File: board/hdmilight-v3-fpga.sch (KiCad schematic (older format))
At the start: 47 parts, among them J3 Conn_01x02_Male, U5 XC6SLX9-TQG144, U7 S25FL064L, X1 SG-310SCF-32MHz

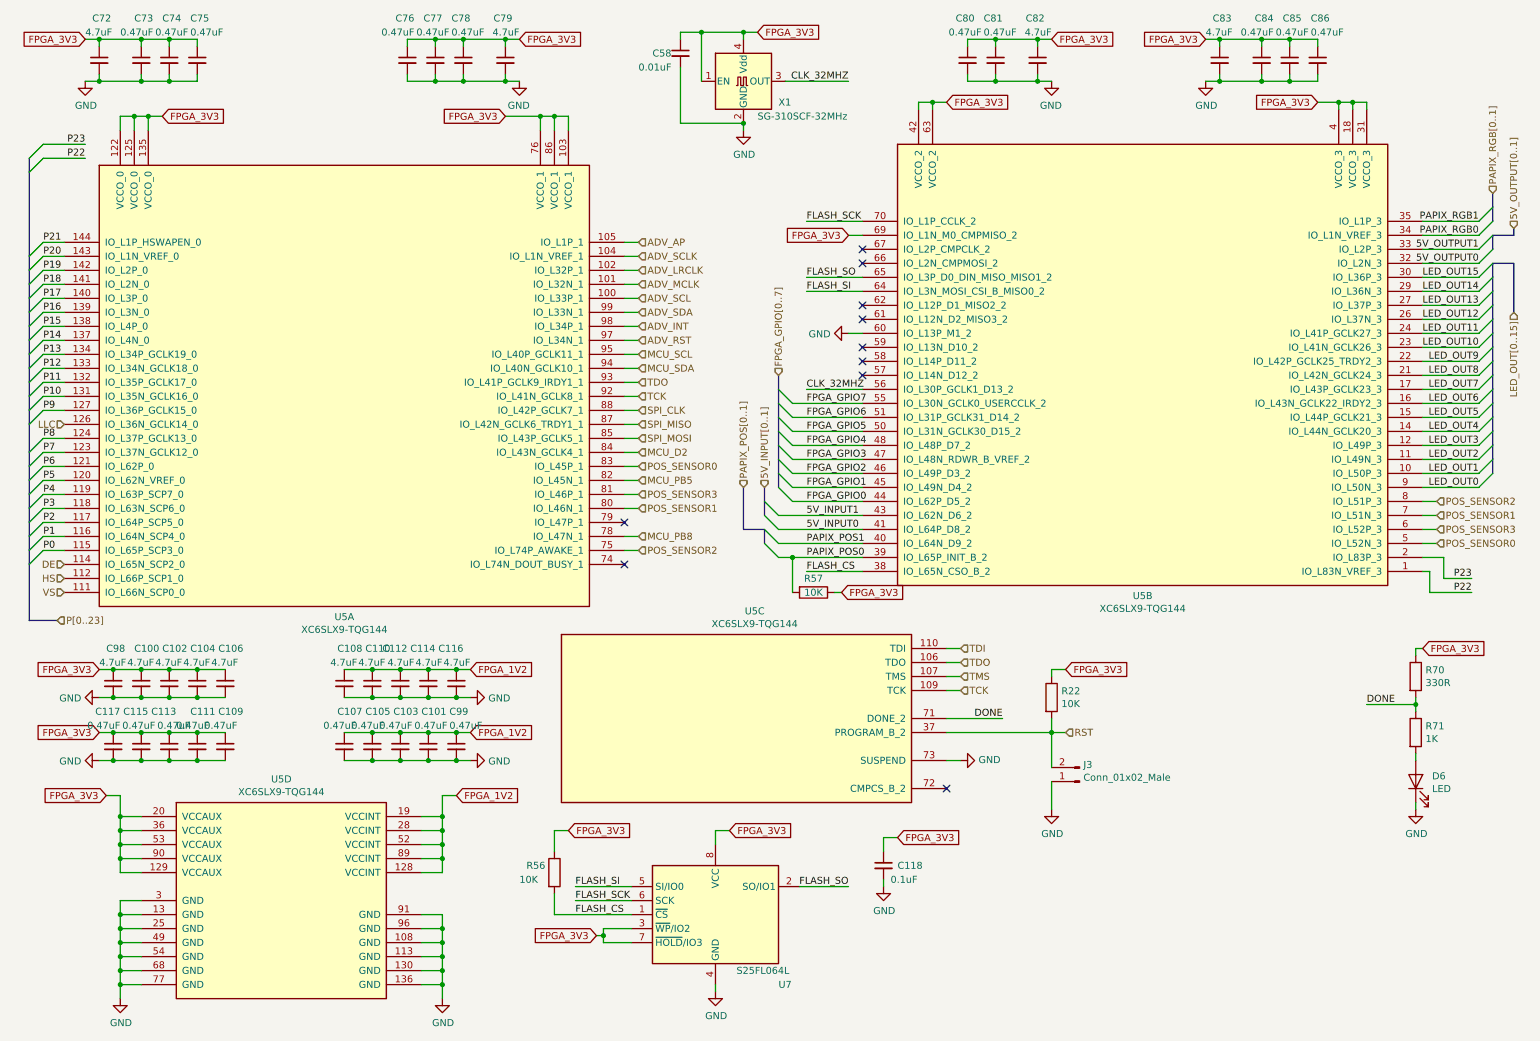
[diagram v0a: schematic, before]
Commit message: Fixed bugs in v3.0 board:
 * Changed FPGA GPIO to 2 row with ground to make it compatible with logic analyser plug for debugging
 * Move position sensor from PB4 to PB5
 * Connect voltage regulator center pad to ground pins
 * Add SPI CS line between FPGA and MCU
 * Move HDMI hotplug LED back from board edge
 * Move HDMI ESD chip closer to connector
 * Swap serial rx/tx
 * Fix FPGA EEPROM footprint
 * Fix reset button footprint
 * Connect ADV I2C to MCU
 * Fix missing ground to hotplug power off circuit
 * Move LED power connector to back of board
 * Move standby button to front of board
 * Only use HDMI 5v for hotplug detect
 * Change LED power switching to high side to stop it grounding back through the data line
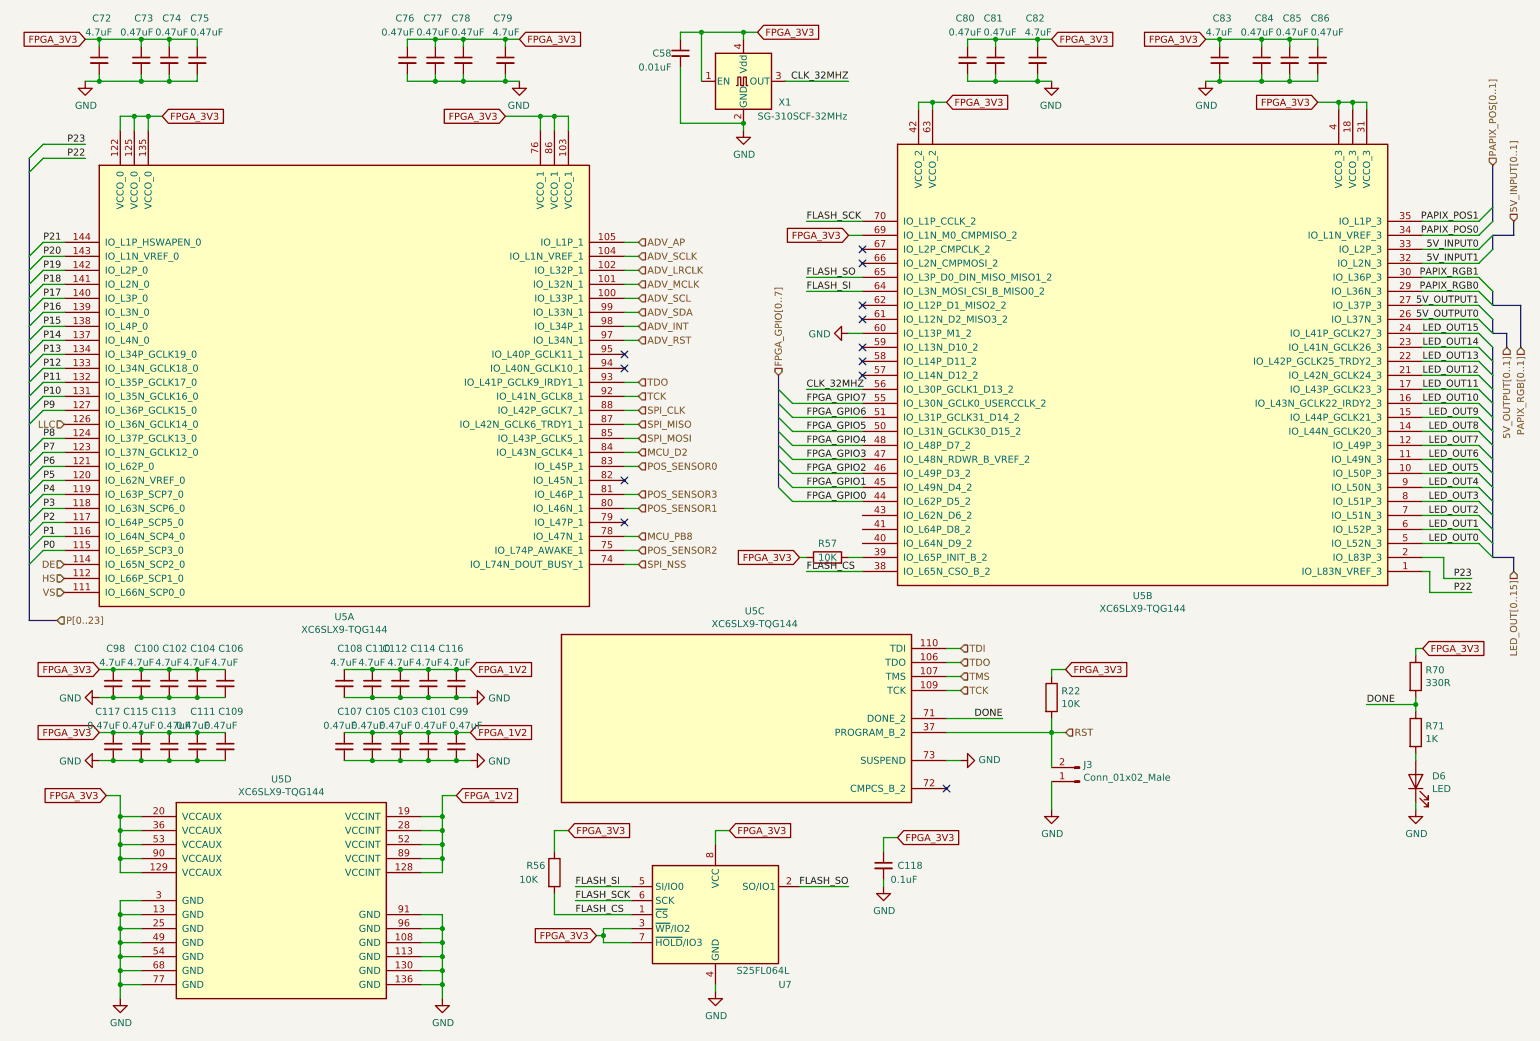
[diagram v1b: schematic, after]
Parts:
- U7: footprint Package_SO:SOIC-8_3.9x4.9mm_P1.27mm -> Package_SO:SOIC-8_5.23x5.23mm_P1.27mm
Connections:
- net 5V_INPUT0: now also U5.33 (IO_L2P_3); no longer U5.41 (IO_L64P_D8_2)
- net 5V_INPUT1: now also U5.32 (IO_L2N_3); no longer U5.43 (IO_L62N_D6_2)
- net 5V_OUTPUT0: now also U5.26 (IO_L37N_3); no longer U5.32 (IO_L2N_3)
- net 5V_OUTPUT1: now also U5.27 (IO_L37P_3); no longer U5.33 (IO_L2P_3)
- net LED_OUT0: now also U5.5 (IO_L52N_3); no longer U5.9 (IO_L50N_3)
- net LED_OUT1: now also U5.6 (IO_L52P_3); no longer U5.10 (IO_L50P_3)
- net LED_OUT10: now also U5.16 (IO_L43N_GCLK22_IRDY2_3); no longer U5.23 (IO_L41N_GCLK26_3)
- net LED_OUT11: now also U5.17 (IO_L43P_GCLK23_3); no longer U5.24 (IO_L41P_GCLK27_3)
- net LED_OUT12: now also U5.21 (IO_L42N_GCLK24_3); no longer U5.26 (IO_L37N_3)
- net LED_OUT13: now also U5.22 (IO_L42P_GCLK25_TRDY2_3); no longer U5.27 (IO_L37P_3)
- net LED_OUT14: now also U5.23 (IO_L41N_GCLK26_3); no longer U5.29 (IO_L36N_3)
- net LED_OUT15: now also U5.24 (IO_L41P_GCLK27_3); no longer U5.30 (IO_L36P_3)
- net LED_OUT2: now also U5.7 (IO_L51N_3); no longer U5.11 (IO_L49N_3)
- net LED_OUT3: now also U5.8 (IO_L51P_3); no longer U5.12 (IO_L49P_3)
- net LED_OUT4: now also U5.9 (IO_L50N_3); no longer U5.14 (IO_L44N_GCLK20_3)
- net LED_OUT5: now also U5.10 (IO_L50P_3); no longer U5.15 (IO_L44P_GCLK21_3)
- net LED_OUT6: now also U5.11 (IO_L49N_3); no longer U5.16 (IO_L43N_GCLK22_IRDY2_3)
- net LED_OUT7: now also U5.12 (IO_L49P_3); no longer U5.17 (IO_L43P_GCLK23_3)
- net LED_OUT8: now also U5.14 (IO_L44N_GCLK20_3); no longer U5.21 (IO_L42N_GCLK24_3)
- net LED_OUT9: now also U5.15 (IO_L44P_GCLK21_3); no longer U5.22 (IO_L42P_GCLK25_TRDY2_3)
- net PAPIX_POS0: now also U5.34 (IO_L1N_VREF_3); no longer R57.2, U5.39 (IO_L65P_INIT_B_2)
- net PAPIX_POS1: now also U5.35 (IO_L1P_3); no longer U5.40 (IO_L64N_D9_2)
- net PAPIX_RGB0: now also U5.29 (IO_L36N_3); no longer U5.34 (IO_L1N_VREF_3)
- net PAPIX_RGB1: now also U5.30 (IO_L36P_3); no longer U5.35 (IO_L1P_3)
- net POS_SENSOR0: no longer U5.5 (IO_L52N_3)
- net POS_SENSOR1: no longer U5.7 (IO_L51N_3)
- net POS_SENSOR2: no longer U5.8 (IO_L51P_3)
- net POS_SENSOR3: no longer U5.6 (IO_L52P_3)
- net SPI_NSS: now reaches U5.74 (IO_L74N_DOUT_BUSY_1)
- net MCU_PB5: no longer names the net of U5.82 (IO_L45N_1)
- net MCU_SCL: no longer names the net of U5.95 (IO_L40P_GCLK11_1)
- net MCU_SDA: no longer names the net of U5.94 (IO_L40N_GCLK10_1)
- new net: R57.2, U5.39 (IO_L65P_INIT_B_2)
- no-connect marks 10 -> 12
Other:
- moved on the sheet: R57
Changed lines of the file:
@@
 F 0 "U7" H 5900 6450 50  0000 L CNN
 F 1 "S25FL064L" H 5600 6550 50  0000 L CNN
-F 2 "Package_SO:SOIC-8_3.9x4.9mm_P1.27mm" H 5450 6350 50  0001 C CNN
+F 2 "Package_SO:SOIC-8_5.23x5.23mm_P1.27mm" H 5450 6350 50  0001 C CNN
 F 3 "" H 5450 6950 50  0001 C CNN
 	1    5450 6950
@@
 	7850 6200 7850 6000
 Wire Wire Line
+	10500 3600 10900 3600
+Wire Wire Line
+	10500 3700 10900 3700
+Wire Wire Line
+	10500 3800 10900 3800
+Wire Wire Line
+	10500 3900 10900 3900
+Wire Wire Line
+	10500 4000 10900 4000
+Wire Wire Line
+	10500 4100 10900 4100
+Wire Wire Line
+	10500 4200 10900 4200
+Wire Wire Line
+	10500 4300 10900 4300
+Entry Wire Line
+	10900 3600 11000 3700
+Entry Wire Line
+	10900 3700 11000 3800
+Entry Wire Line
+	10900 3800 11000 3900
+Entry Wire Line
+	10900 3900 11000 4000
+Entry Wire Line
+	10900 4000 11000 4100
+Entry Wire Line
+	10900 4100 11000 4200
+Entry Wire Line
+	10900 4200 11000 4300
+Entry Wire Line
+	10900 4300 11000 4400
+Wire Wire Line
+	10500 3500 10900 3500
+Wire Wire Line
+	10500 3400 10900 3400
+Wire Wire Line
+	10500 3300 10900 3300
+Wire Wire Line
 	10500 3200 10900 3200
 Wire Wire Line
-	10500 3300 10900 3300
-Wire Wire Line
-	10500 3400 10900 3400
-Wire Wire Line
-	10500 3500 10900 3500
-Wire Wire Line
-	10500 3600 10900 3600
-Wire Wire Line
-	10500 3700 10900 3700
-Wire Wire Line
-	10500 3800 10900 3800
-Wire Wire Line
-	10500 3900 10900 3900
-Entry Wire Line
-	10900 3200 11000 3100
-Entry Wire Line
-	10900 3300 11000 3200
-Entry Wire Line
-	10900 3400 11000 3300
-Entry Wire Line
-	10900 3500 11000 3400
-Entry Wire Line
-	10900 3600 11000 3500
-Entry Wire Line
-	10900 3700 11000 3600
-Entry Wire Line
-	10900 3800 11000 3700
-Entry Wire Line
-	10900 3900 11000 3800
-Wire Wire Line
 	10500 3100 10900 3100
 Wire Wire Line
@@
 Wire Wire Line
 	10500 2800 10900 2800
-Wire Wire Line
-	10500 2700 10900 2700
-Wire Wire Line
-	10500 2600 10900 2600
+Entry Wire Line
+	10900 3500 11000 3600
+Entry Wire Line
+	10900 3400 11000 3500
+Entry Wire Line
+	10900 3300 11000 3400
+Entry Wire Line
+	10900 3200 11000 3300
+Entry Wire Line
+	10900 3100 11000 3200
+Entry Wire Line
+	10900 3000 11000 3100
+Entry Wire Line
+	10900 2900 11000 3000
+Entry Wire Line
+	10900 2800 11000 2900
+Text Label 10900 2800 2    50   ~ 0
+LED_OUT15
+Text Label 10900 2900 2    50   ~ 0
+LED_OUT14
+Text Label 10900 3000 2    50   ~ 0
+LED_OUT13
+Text Label 10900 3100 2    50   ~ 0
+LED_OUT12
+Text Label 10900 3200 2    50   ~ 0
+LED_OUT11
+Text Label 10900 3300 2    50   ~ 0
+LED_OUT10
+Text Label 10900 3400 2    50   ~ 0
+LED_OUT9
+Text Label 10900 3500 2    50   ~ 0
+LED_OUT8
+Text Label 10900 3600 2    50   ~ 0
+LED_OUT7
+Text Label 10900 3700 2    50   ~ 0
+LED_OUT6
+Text Label 10900 3800 2    50   ~ 0
+LED_OUT5
+Text Label 10900 3900 2    50   ~ 0
+LED_OUT4
+Text Label 10900 4000 2    50   ~ 0
+LED_OUT3
+Text Label 10900 4100 2    50   ~ 0
+LED_OUT2
+Text Label 10900 4200 2    50   ~ 0
+LED_OUT1
+Text Label 10900 4300 2    50   ~ 0
+LED_OUT0
+Text HLabel 11150 4500 3    50   Input ~ 0
+LED_OUT[0..15]
 Wire Wire Line
 	10500 2500 10900 2500
 Wire Wire Line
 	10500 2400 10900 2400
-Entry Wire Line
-	10900 3100 11000 3000
-Entry Wire Line
-	10900 3000 11000 2900
-Entry Wire Line
-	10900 2900 11000 2800
-Entry Wire Line
-	10900 2800 11000 2700
-Entry Wire Line
-	10900 2700 11000 2600
-Entry Wire Line
-	10900 2600 11000 2500
-Entry Wire Line
-	10900 2500 11000 2400
-Entry Wire Line
-	10900 2400 11000 2300
+Text Label 10900 2500 2    50   ~ 0
+PAPIX_RGB0
 Text Label 10900 2400 2    50   ~ 0
-LED_OUT15
-Text Label 10900 2500 2    50   ~ 0
-LED_OUT14
-Text Label 10900 2600 2    50   ~ 0
-LED_OUT13
-Text Label 10900 2700 2    50   ~ 0
-LED_OUT12
-Text Label 10900 2800 2    50   ~ 0
-LED_OUT11
-Text Label 10900 2900 2    50   ~ 0
-LED_OUT10
-Text Label 10900 3000 2    50   ~ 0
-LED_OUT9
-Text Label 10900 3100 2    50   ~ 0
-LED_OUT8
-Text Label 10900 3200 2    50   ~ 0
-LED_OUT7
-Text Label 10900 3300 2    50   ~ 0
-LED_OUT6
-Text Label 10900 3400 2    50   ~ 0
-LED_OUT5
-Text Label 10900 3500 2    50   ~ 0
-LED_OUT4
-Text Label 10900 3600 2    50   ~ 0
-LED_OUT3
-Text Label 10900 3700 2    50   ~ 0
-LED_OUT2
-Text Label 10900 3800 2    50   ~ 0
-LED_OUT1
-Text Label 10900 3900 2    50   ~ 0
-LED_OUT0
-Wire Bus Line
-	11000 2300 11150 2300
-Text HLabel 11150 2650 3    50   Input ~ 0
-LED_OUT[0..15]
-Wire Wire Line
-	10500 2100 10900 2100
-Wire Wire Line
-	10500 2000 10900 2000
-Text Label 10900 2100 2    50   ~ 0
-PAPIX_RGB0
-Text Label 10900 2000 2    50   ~ 0
 PAPIX_RGB1
 Entry Wire Line
-	10900 2000 11000 1900
-Entry Wire Line
-	10900 2100 11000 2000
-Text HLabel 11000 1800 1    50   Input ~ 0
+	10900 2400 11000 2500
+Entry Wire Line
+	10900 2500 11000 2600
+Text HLabel 11200 2900 3    50   Input ~ 0
 PAPIX_RGB[0..1]
 Wire Wire Line
@@
 Wire Wire Line
 	5350 650  5650 650
-Wire Wire Line
-	10500 4100 10600 4100
-Wire Wire Line
-	10500 4200 10600 4200
-Wire Wire Line
-	10500 4300 10600 4300
 Text HLabel 4900 3750 2    50   Input ~ 0
 POS_SENSOR0
@@
 POS_SENSOR1
 Text HLabel 4900 4350 2    50   Input ~ 0
-POS_SENSOR2
-Wire Wire Line
-	10500 4000 10600 4000
-Text HLabel 10600 4300 2    50   Input ~ 0
-POS_SENSOR0
-Text HLabel 10600 4200 2    50   Input ~ 0
-POS_SENSOR3
-Text HLabel 10600 4100 2    50   Input ~ 0
-POS_SENSOR1
-Text HLabel 10600 4000 2    50   Input ~ 0
 POS_SENSOR2
 $Comp
@@
 Text HLabel 4900 2150 2    50   Input ~ 0
 ADV_AP
-Text HLabel 4900 3050 2    50   Input ~ 0
-MCU_SDA
-Text HLabel 4900 2950 2    50   Input ~ 0
-MCU_SCL
 Wire Wire Line
 	4800 2150 4900 2150
@@
 Wire Wire Line
 	4800 2850 4900 2850
-Wire Wire Line
-	4800 2950 4900 2950
-Wire Wire Line
-	4800 3050 4900 3050
 Wire Wire Line
 	4800 3350 4900 3350
@@
 Text HLabel 4900 3650 2    50   Input ~ 0
 MCU_D2
-Text HLabel 4900 3850 2    50   Input ~ 0
-MCU_PB5
 Text HLabel 4900 4250 2    50   Input ~ 0
 MCU_PB8
 Wire Wire Line
 	4800 4250 4900 4250
-Wire Wire Line
-	4800 3850 4900 3850
 Wire Wire Line
 	4800 3650 4900 3650
@@
 	7850 5650 7950 5650
 Entry Wire Line
-	10900 2300 11000 2200
-Wire Bus Line
-	11000 2100 11150 2100
-Entry Wire Line
-	10900 2200 11000 2100
-Text HLabel 11150 2050 1    50   Input ~ 0
+	10900 2700 11000 2800
+Entry Wire Line
+	10900 2600 11000 2700
+Text HLabel 11100 2900 3    50   Input ~ 0
 5V_OUTPUT[0..1]
-Text Label 10900 2200 2    50   ~ 0
+Text Label 10900 2600 2    50   ~ 0
 5V_OUTPUT1
-Text Label 10900 2300 2    50   ~ 0
+Text Label 10900 2700 2    50   ~ 0
 5V_OUTPUT0
 Wire Wire Line
-	10500 2200 10900 2200
-Wire Wire Line
-	10500 2300 10900 2300
-Wire Wire Line
-	6500 4400 6000 4400
-Wire Wire Line
-	6500 4300 5900 4300
-Entry Wire Line
-	5800 4300 5900 4400
-Entry Wire Line
-	5800 4200 5900 4300
-Text Label 6100 4400 0    50   ~ 0
+	10500 2600 10900 2600
+Wire Wire Line
+	10500 2700 10900 2700
+Text Label 10900 2100 2    50   ~ 0
 PAPIX_POS0
-Text Label 6100 4300 0    50   ~ 0
+Text Label 10900 2000 2    50   ~ 0
 PAPIX_POS1
-Wire Bus Line
-	5650 4200 5800 4200
-Text HLabel 5650 3900 1    50   Input ~ 0
-PAPIX_POS[0..1]
 Wire Wire Line
 	6500 3900 6000 3900
@@
 L Device:R R57
 U 1 1 60AF6D65
-P 6150 4650
-F 0 "R57" V 6050 4650 50  0000 C CNN
-F 1 "10K" V 6150 4650 50  0000 C CNN
-F 2 "Resistor_SMD:R_0603_1608Metric" V 6080 4650 50  0001 C CNN
-F 3 "~" H 6150 4650 50  0001 C CNN
-	1    6150 4650
-	0    1    1    0
-$EndComp
-Text GLabel 6350 4650 2    50   Input ~ 0
-FPGA_3V3
-Wire Wire Line
-	6300 4650 6350 4650
-Wire Wire Line
-	6000 4650 6000 4400
-Connection ~ 6000 4400
-Wire Wire Line
-	6000 4400 5900 4400
+P 6250 4400
+F 0 "R57" V 6350 4400 50  0000 C CNN
+F 1 "10K" V 6250 4400 50  0000 C CNN
+F 2 "Resistor_SMD:R_0603_1608Metric" V 6180 4400 50  0001 C CNN
+F 3 "~" H 6250 4400 50  0001 C CNN
+	1    6250 4400
+	0    -1   -1   0
+$EndComp
+Text GLabel 6050 4400 0    50   Input ~ 0
+FPGA_3V3
+Wire Wire Line
+	6100 4400 6050 4400
 Wire Wire Line
 	4300 6350 4400 6350
 Wire Wire Line
 	4450 6850 4850 6850
-Wire Wire Line
-	6500 4100 5900 4100
-Text Label 6100 4100 0    50   ~ 0
+Text Label 10900 2300 2    50   ~ 0
 5V_INPUT1
-Text Label 6100 4200 0    50   ~ 0
+Text Label 10900 2200 2    50   ~ 0
 5V_INPUT0
 $Comp
@@
 NoConn ~ 6500 3100
 NoConn ~ 4800 4150
-NoConn ~ 4800 4450
 NoConn ~ 7100 6050
 Wire Wire Line
@@
 Wire Wire Line
 	6000 4000 6500 4000
-Wire Wire Line
-	6500 4200 5900 4200
-Text HLabel 5800 3900 1    50   Input ~ 0
+Wire Bus Line
+	11000 2700 11000 2800
+Entry Wire Line
+	11000 2100 10900 2200
+Entry Wire Line
+	11000 2200 10900 2300
+Text HLabel 11150 2000 1    50   Input ~ 0
 5V_INPUT[0..1]
-Entry Wire Line
-	5800 4100 5900 4200
-Entry Wire Line
-	5800 4000 5900 4100
+Text HLabel 11000 1600 1    50   Input ~ 0
+PAPIX_POS[0..1]
+Entry Wire Line
+	11000 1900 10900 2000
+Entry Wire Line
+	11000 2000 10900 2100
 Wire Bus Line
-	5800 4200 5800 4300
+	11000 4400 11150 4400
 Wire Bus Line
-	5650 3900 5650 4200
+	11150 4400 11150 4500
 Wire Bus Line
-	11150 2050 11150 2100
+	11000 2800 11100 2800
+Wire Bus Line
+	11100 2800 11100 2900
+Wire Bus Line
+	11000 2500 11000 2600
+Wire Bus Line
+	11000 2600 11200 2600
+Wire Bus Line
+	11200 2600 11200 2900
+Wire Wire Line
+	10500 2100 10900 2100
+Wire Wire Line
+	10500 2300 10900 2300
+Wire Wire Line
+	10500 2200 10900 2200
+Wire Wire Line
+	10500 2000 10900 2000
+Wire Wire Line
+	6400 4400 6500 4400
+Wire Wire Line
+	4800 4450 4900 4450
+Text HLabel 4900 4450 2    50   Input ~ 0
+SPI_NSS
+NoConn ~ 4800 2950
+NoConn ~ 4800 3050
+NoConn ~ 4800 3850
+Wire Bus Line
+	11000 2100 11150 2100
+Wire Bus Line
+	11150 2100 11150 2000
 Wire Bus Line
 	11000 2100 11000 2200
 Wire Bus Line
-	11150 2300 11150 2650
-Wire Bus Line
-	11000 1800 11000 2000
-Wire Bus Line
-	5800 3900 5800 4100
+	11000 1600 11000 2000
 Wire Bus Line
 	5900 3100 5900 3900
 Wire Bus Line
-	11000 2300 11000 3800
+	11000 2900 11000 4400
 Wire Bus Line
 	550  1550 550  4850

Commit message: Updated BOM with individual LED colours/types
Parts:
- D6: value LED -> LED Red
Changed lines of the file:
@@
 P 10450 6000
 F 0 "D6" V 10489 5883 50  0000 R CNN
-F 1 "LED" V 10398 5883 50  0000 R CNN
+F 1 "LED Red" V 10398 5883 50  0000 R CNN
 F 2 "LED_SMD:LED_0603_1608Metric" H 10450 6000 50  0001 C CNN
 F 3 "~" H 10450 6000 50  0001 C CNN
